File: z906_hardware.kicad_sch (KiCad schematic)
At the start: 16 parts, among them J1 USB_C_Receptacle_USB2.0_14P, J3 DE_15 Amplifier, J4 DE15 Console, U1 ESP32-S3-WROOM-1, U2 ME6211C33M5, U3 PCM5102A

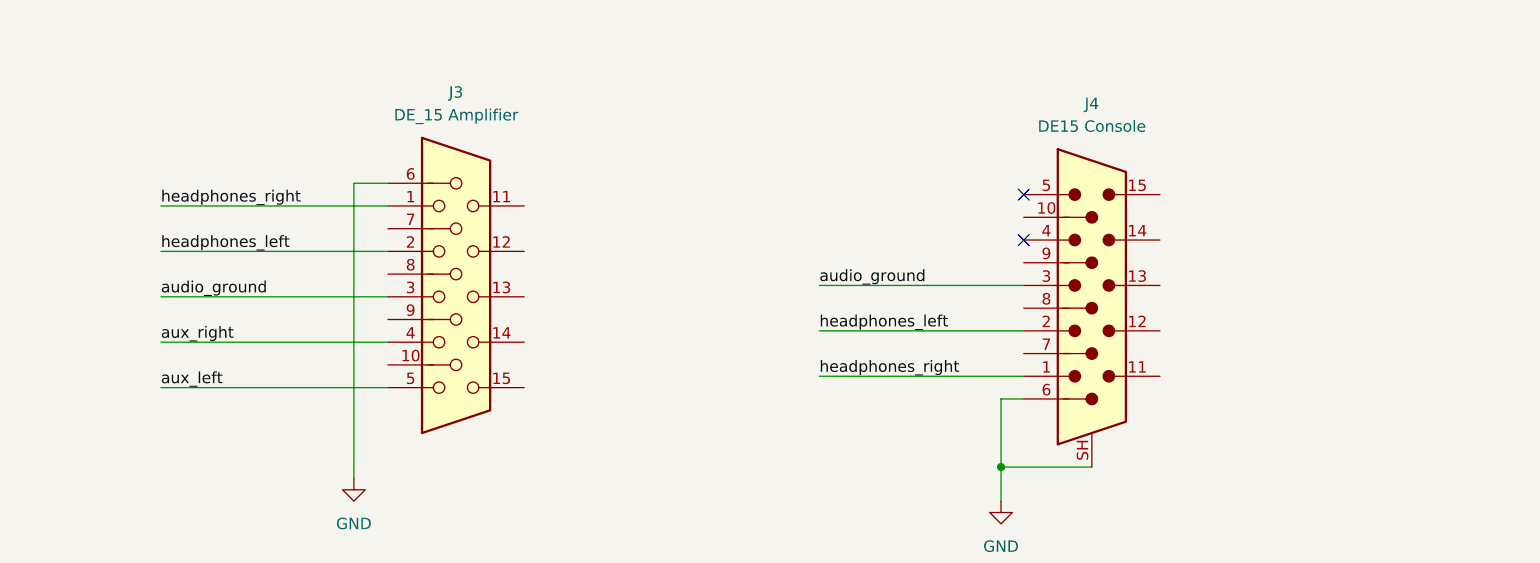
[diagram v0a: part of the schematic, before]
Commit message: dsub connection
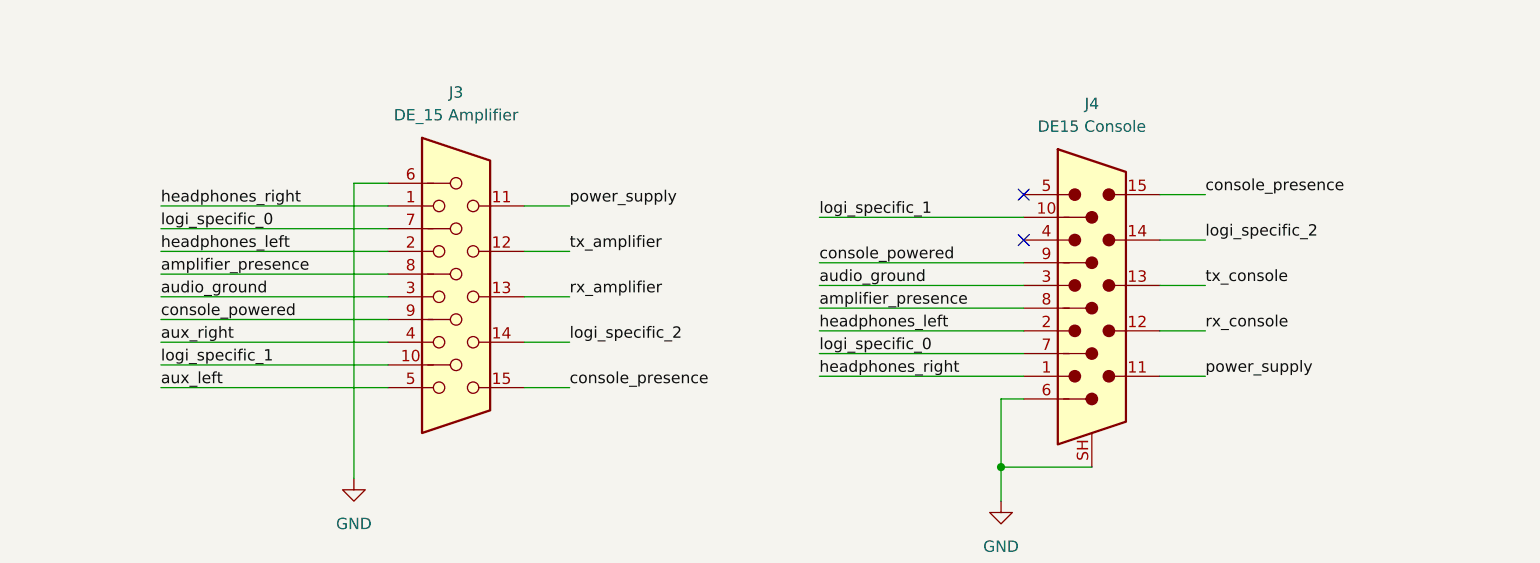
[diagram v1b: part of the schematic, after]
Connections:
- net logi_specific_1: now reaches J3.10
- net logi_specific_1: now also J4.10
- net power_supply: now reaches J3.11
- net power_supply: now also J4.11
- net tx_amplifier: now reaches J3.12
- net rx_amplifier: now reaches J3.13
- net logi_specific_2: now reaches J3.14
- net logi_specific_2: now also J4.14
- net console_presence: now reaches J3.15
- net console_presence: now also J4.15
- net logi_specific_0: now reaches J3.7
- net logi_specific_0: now also J4.7
- net amplifier_presence: now reaches J3.8
- net amplifier_presence: now also J4.8
- net console_powered: now reaches J3.9
- net console_powered: now also J4.9
- net rx_console: now reaches J4.12
- net tx_console: now reaches J4.13

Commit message: esp32-s3
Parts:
- added C4, C7: 0.1uF/50V(10%), symbol Device:C
- added C5, C6: 10uF/25V(20%), symbol Device:C
- added C8: 1uF/16V(10%), symbol Device:C
- added D5: LED, symbol Device:LED
- added R3: 5.1K(1%), symbol Device:R
- added R4: 0, symbol Device:R
- added R5: 10K(1%), symbol Device:R
- C2: value C -> 10uF/25V(20%)
- C3: value C -> 0.1uF/50V(10%)
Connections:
- net GND: now also C4.2, C5.2, C6.2, C7.2, C8.2, D5.1 (K)
- net GPIO19: now also U1.13 (USB_D-); no longer U1.14 (USB_D+)
- net GPIO20: now also U1.14 (USB_D+); no longer U1.23 (IO21)
- net amplifier_presence: now also U1.4 (IO4)
- net console_powered: now also U1.12 (IO8)
- net console_presence: now also U1.17 (IO9)
- net rx_amplifier: now also U1.11 (IO18)
- net rx_console: now also U1.8 (IO15)
- net tx_amplifier: now also U1.10 (IO17)
- net tx_console: now also U1.9 (IO16)
- net +3.3V: now reaches U4.2 (VOUT)
- net +3.3V: now also C4.1, C5.1, C6.1, C7.1, R3.1, R4.2
- net at U1.2 (3V3): now also R4.1, R5.2
- net GPIO0: now reaches U1.27 (IO0)
- net chip_pu: now reaches U1.3 (EN)
- net chip_pu: now also C8.1, R5.1
- new net: D5.2 (A), R3.2
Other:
- moved on the sheet: C2, C3, J3, J4, U1, U2, U3, U4

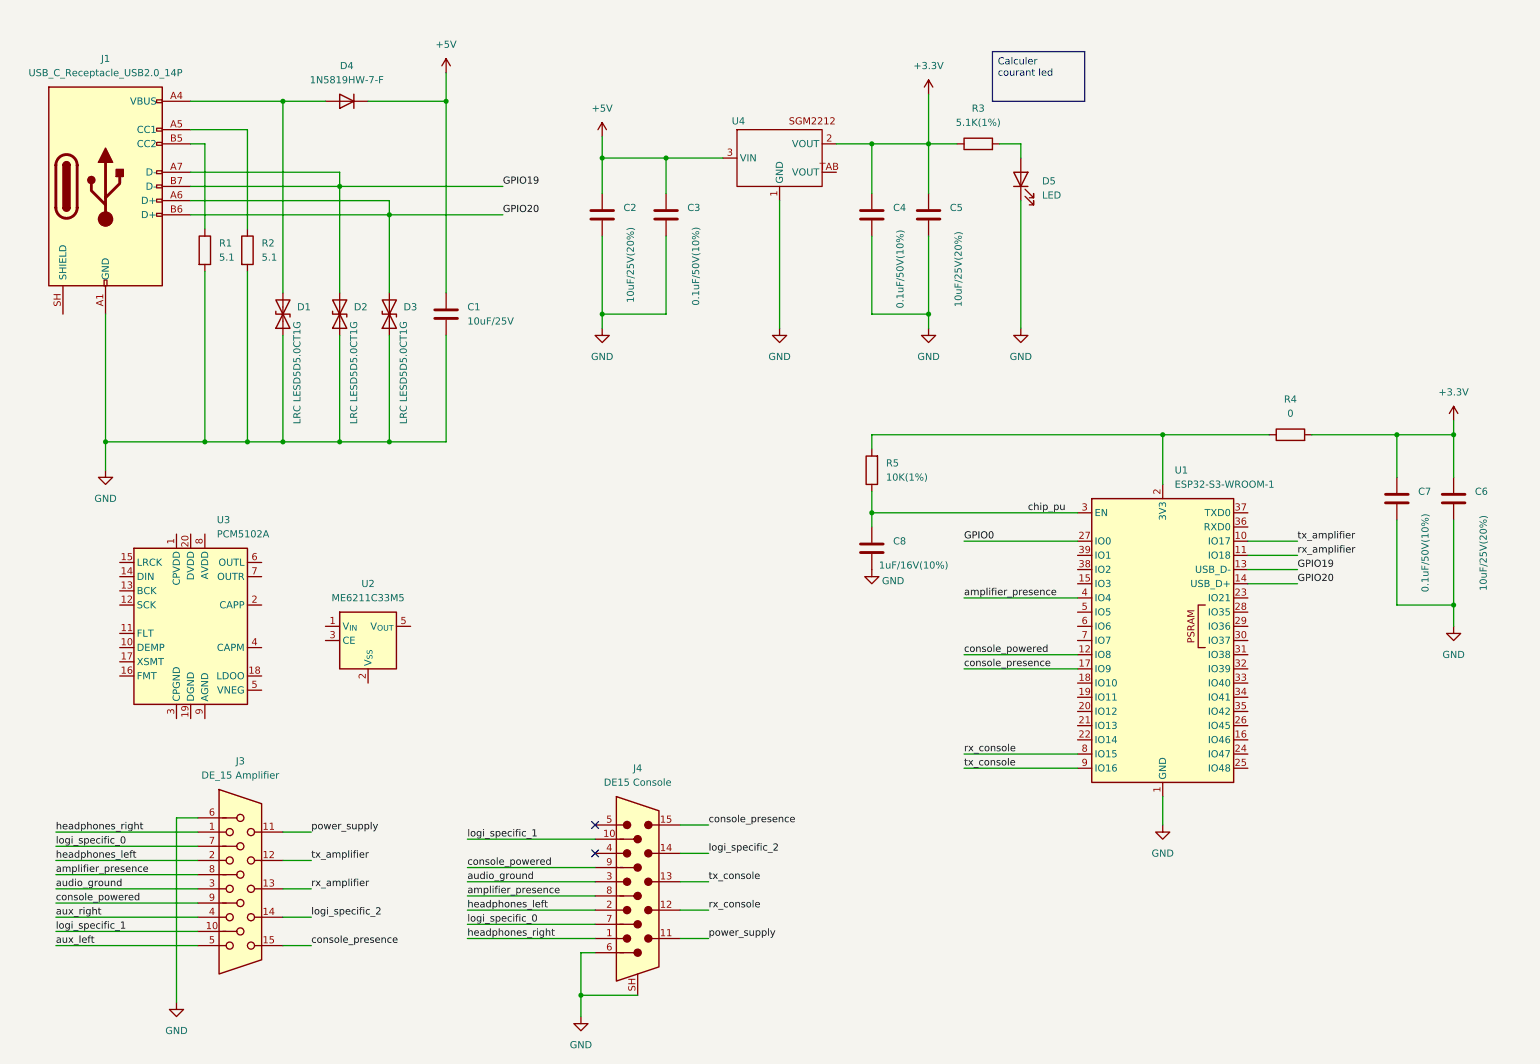
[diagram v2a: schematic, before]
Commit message: change dc-dc power
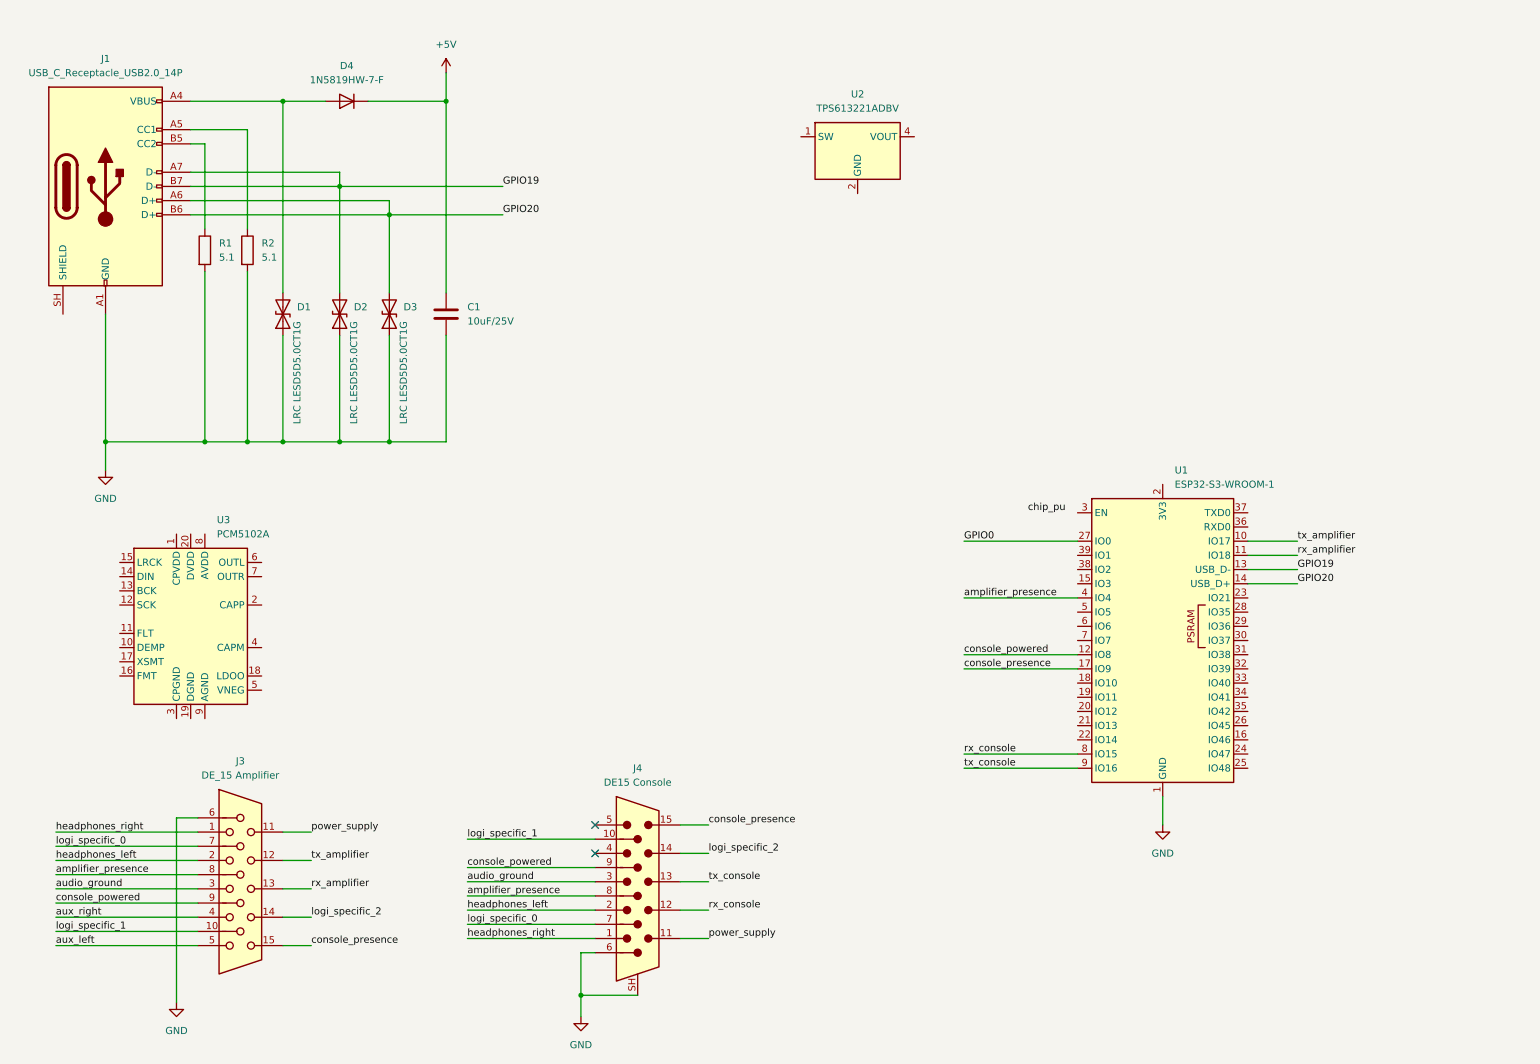
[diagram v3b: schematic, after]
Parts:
- removed C2, C5, C6: 10uF/25V(20%), symbol Device:C
- removed C3, C4, C7: 0.1uF/50V(10%), symbol Device:C
- removed C8: 1uF/16V(10%), symbol Device:C
- removed D5: LED, symbol Device:LED
- removed R3: 5.1K(1%), symbol Device:R
- removed R4: 0, symbol Device:R
- removed R5: 10K(1%), symbol Device:R
- removed U2: ME6211C33M5, Package_TO_SOT_SMD:SOT-23-5, symbol Regulator_Linear:ME6211C33M5
- removed U4: (no value), symbol lib:SGM2212
- added U2: TPS613221ADBV, Package_TO_SOT_SMD:SOT-23-5, symbol Regulator_Switching:TPS613221ADBV
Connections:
- net chip_pu: no longer U1.3 (EN)

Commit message: usb input
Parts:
- removed D1, D2, D3: LRC LESD5D5.0CT1G, Diode_SMD:D_SOD-523, symbol Device:D_TVS
- removed D4: 1N5819HW-7-F, symbol Device:D
- removed U2: TPS613221ADBV, Package_TO_SOT_SMD:SOT-23-5, symbol Regulator_Switching:TPS613221ADBV
- added U2: AP63203WU, Package_TO_SOT_SMD:TSOT-23-6, symbol Regulator_Switching:AP63203WU
- added U4: TPD2EUSB30, Package_TO_SOT_SMD:Texas_DRT-3, symbol Power_Protection:TPD2EUSB30
- added U5: TPD1E05U06DYA, Diode_SMD:D_SOD-523, symbol Power_Protection:TPD1E05U06DYA
- added U6: TPS7A45xxKTT, Package_TO_SOT_SMD:TO-263-5_TabPin3, symbol Regulator_Linear:TPS7A45xxKTT
- C1: value 10uF/25V -> 10uF
- R1, R2: value 5.1 -> 5.1k
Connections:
- net +5V is gone; now on an unnamed net: C1.1
- net GND: now also J1.SH (SHIELD), U4.3 (GND), U5.2 (GND)
- net GPIO19: now also U4.2 (D-)
- net GPIO20: now also U4.1 (D+)
- net at J1.A4 (VBUS), J1.A9 (VBUS), J1.B4 (VBUS)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: now also U5.1 (I/O)

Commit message: numeric alimentation
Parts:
- added C2: 10uF, symbol Device:C
- added C3: 100nF, symbol Device:C
- added C4: 22uF, symbol Device:C
- added C5: 20uF, symbol Device:C
- added L1: 3.9uH (3A), symbol Device:L
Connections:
- net GND: now also U2.4 (GND), C2.2, C4.2, C5.2
- net +5V: now reaches C1.1, J1.A4 (VBUS), J1.A9 (VBUS), J1.B4 (VBUS), J1.B9 (VBUS), U5.1 (I/O)
- net +5V: now also U2.2 (EN), U2.3 (IN), C2.1
- net +3.3V: now reaches U2.1 (FB)
- net +3.3V: now also C4.1, C5.1, L1.2
- net at U2.5 (SW): now also C3.1, L1.1
- net at U2.6 (BST): now also C3.2
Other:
- moved on the sheet: U2

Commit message: analog power
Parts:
- added C6, C7: 10uF, symbol Device:C
- U6: value TPS7A45xxKTT -> TPS7A4533
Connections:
- net +5V: now also U6.1 (~{SHDN}), U6.2 (IN), C6.1
- net GND: now also C6.2, C7.2
- net +3.3VA: now reaches U6.4 (OUT)
- net +3.3VA: now also U6.5 (SENSE), C7.1
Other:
- moved on the sheet: C3, C4, C5, L1, U6

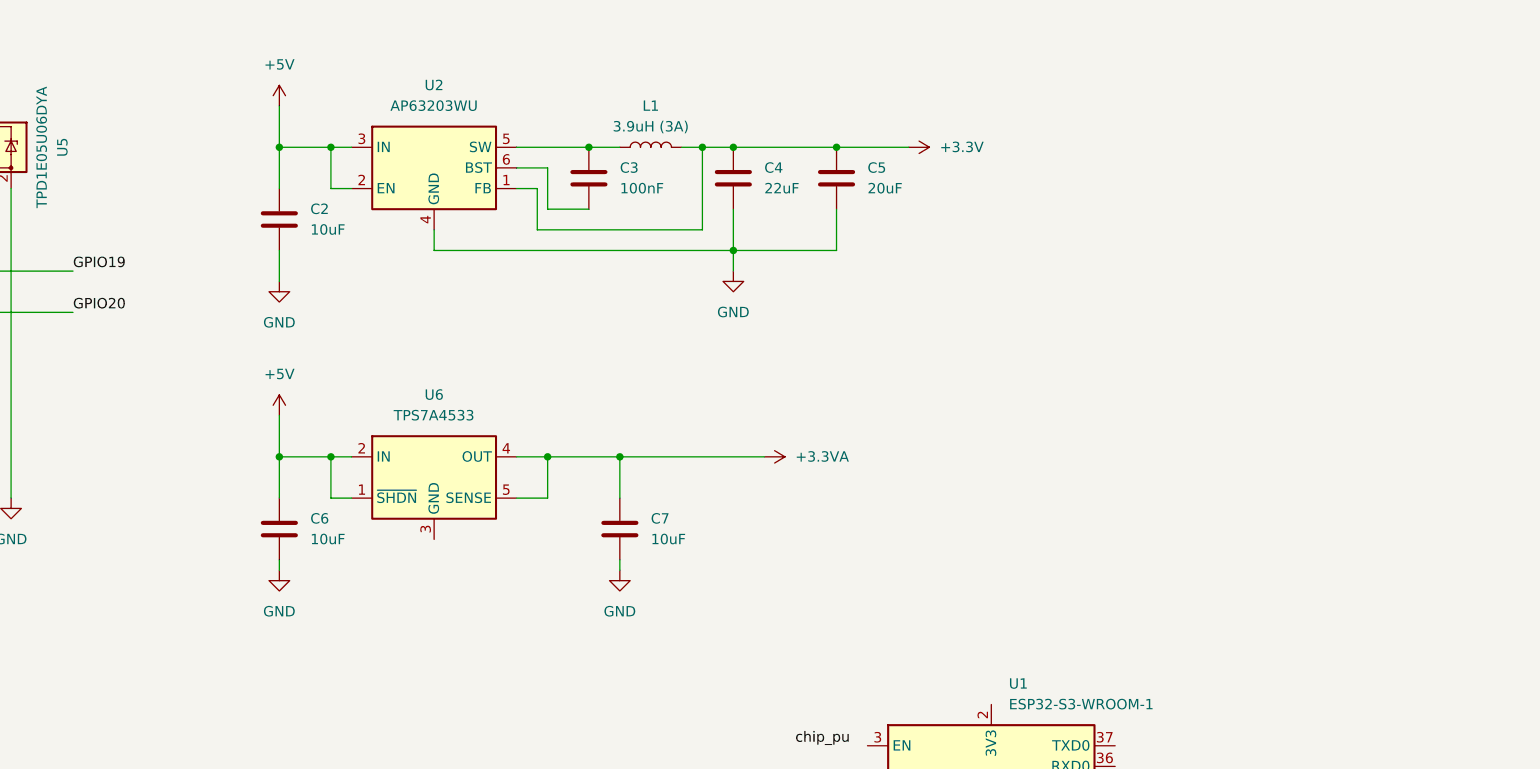
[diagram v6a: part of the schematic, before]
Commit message: add filter to analog power
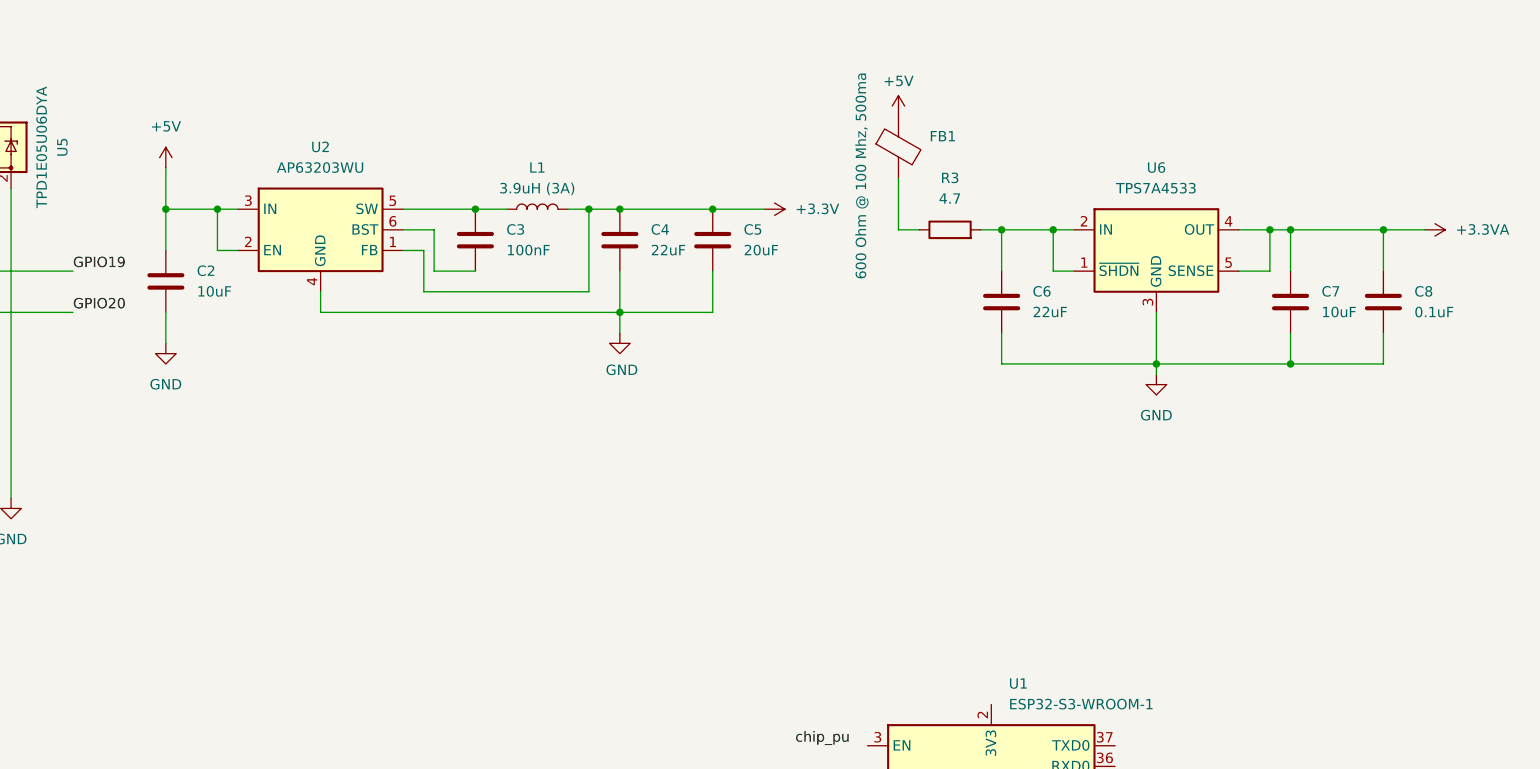
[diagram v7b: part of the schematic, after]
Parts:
- added C8: 0.1uF, symbol Device:C
- added FB1: 600 Ohm @ 100 Mhz, 500ma, symbol Device:FerriteBead
- added R3: 4.7, symbol Device:R
- C6: value 10uF -> 22uF
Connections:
- net +3.3VA: now also C8.1
- net +5V: now also FB1.1; no longer C6.1, U6.1 (~{SHDN}), U6.2 (IN)
- net GND: now also U6.3 (GND), C8.2
- new net: C6.1, R3.2, U6.1 (~{SHDN}), U6.2 (IN)
- new net: FB1.2, R3.1
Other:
- moved on the sheet: C2, C3, C4, C5, C6, C7, L1, U2, U6
